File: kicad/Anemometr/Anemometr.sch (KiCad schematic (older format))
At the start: 74 parts, among them J1 Conn_01x01_Female, J10 Z3, J11 Z3, J12 Z4, J13 Z4, J14 SWD, J15 SWC, J16 +12v, J17 GND, J2 Conn_01x01_Female, J3 RST, J4 TxD, J5 RxD, J6 Z1, J7 Z1, J8 Z2, J9 Z2, U1 TS5A3166DBVR, U2 LMV7239, U3 TS5A3166DBVR, U4 TS5A3166DBVR, U5 STM32F103C8Tx, U6 TS5A3166DBVR, U7 LM2734Y, U8 MCP1700-5002E_SOT23, U9 MCP1700-3002E_SOT23, Y1 8MHz

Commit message: изменено:      kicad/Anemometr/Anemometr-cache.lib 	изменено:      kicad/Anemometr/Anemometr.sch 	изменено:      kicad/Anemometr/Anemometr.sch-bak
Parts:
- added C? (x2): 10p, Capacitor_SMD:C_0603_1608Metric, symbol Device:C
- added D?: W5500, Package_QFP:LQFP-48_7x7mm_P0.5mm, symbol My_Library:W5500
- added Y?: 8MHz, Crystal:Crystal_SMD_Qantek_QC5CB-2Pin_5x3.2mm, symbol Device:Crystal
- D1: symbol My_Library:MAX4477 -> Anemometr-rescue:MAX4477-My_Library
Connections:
- net labels added: +3.3VA
- wire segments 145 -> 151
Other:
- moved on the sheet: C1, C10, C11, C12, C13, C14, C15, C16, C17, C18, C19, C2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

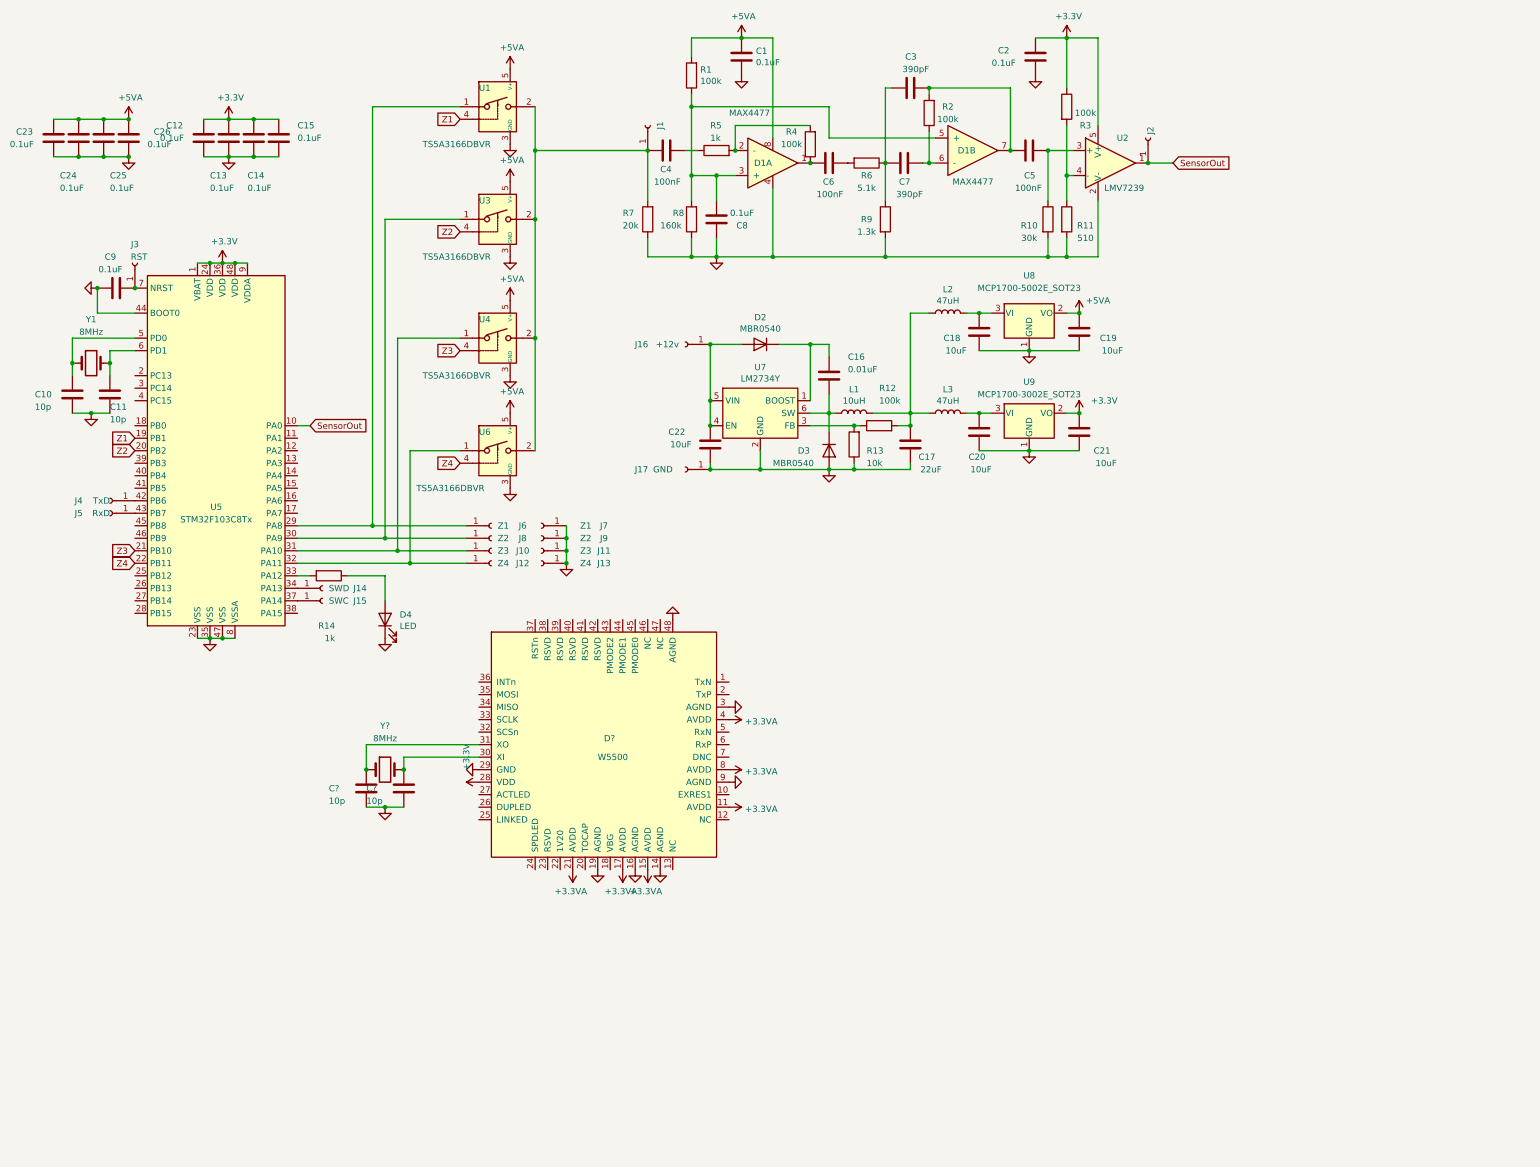
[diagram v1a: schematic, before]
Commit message: изменено:      kicad/Anemometr/Anemometr-cache.lib 	изменено:      kicad/Anemometr/Anemometr.kicad_pcb 	изменено:      kicad/Anemometr/Anemometr.kicad_pcb-bak 	изменено:      kicad/Anemometr/Anemometr.sch 	изменено:      kicad/Anemometr/Anemometr.sch-bak 	изменено:      kicad/Anemometr/fp-info-cache
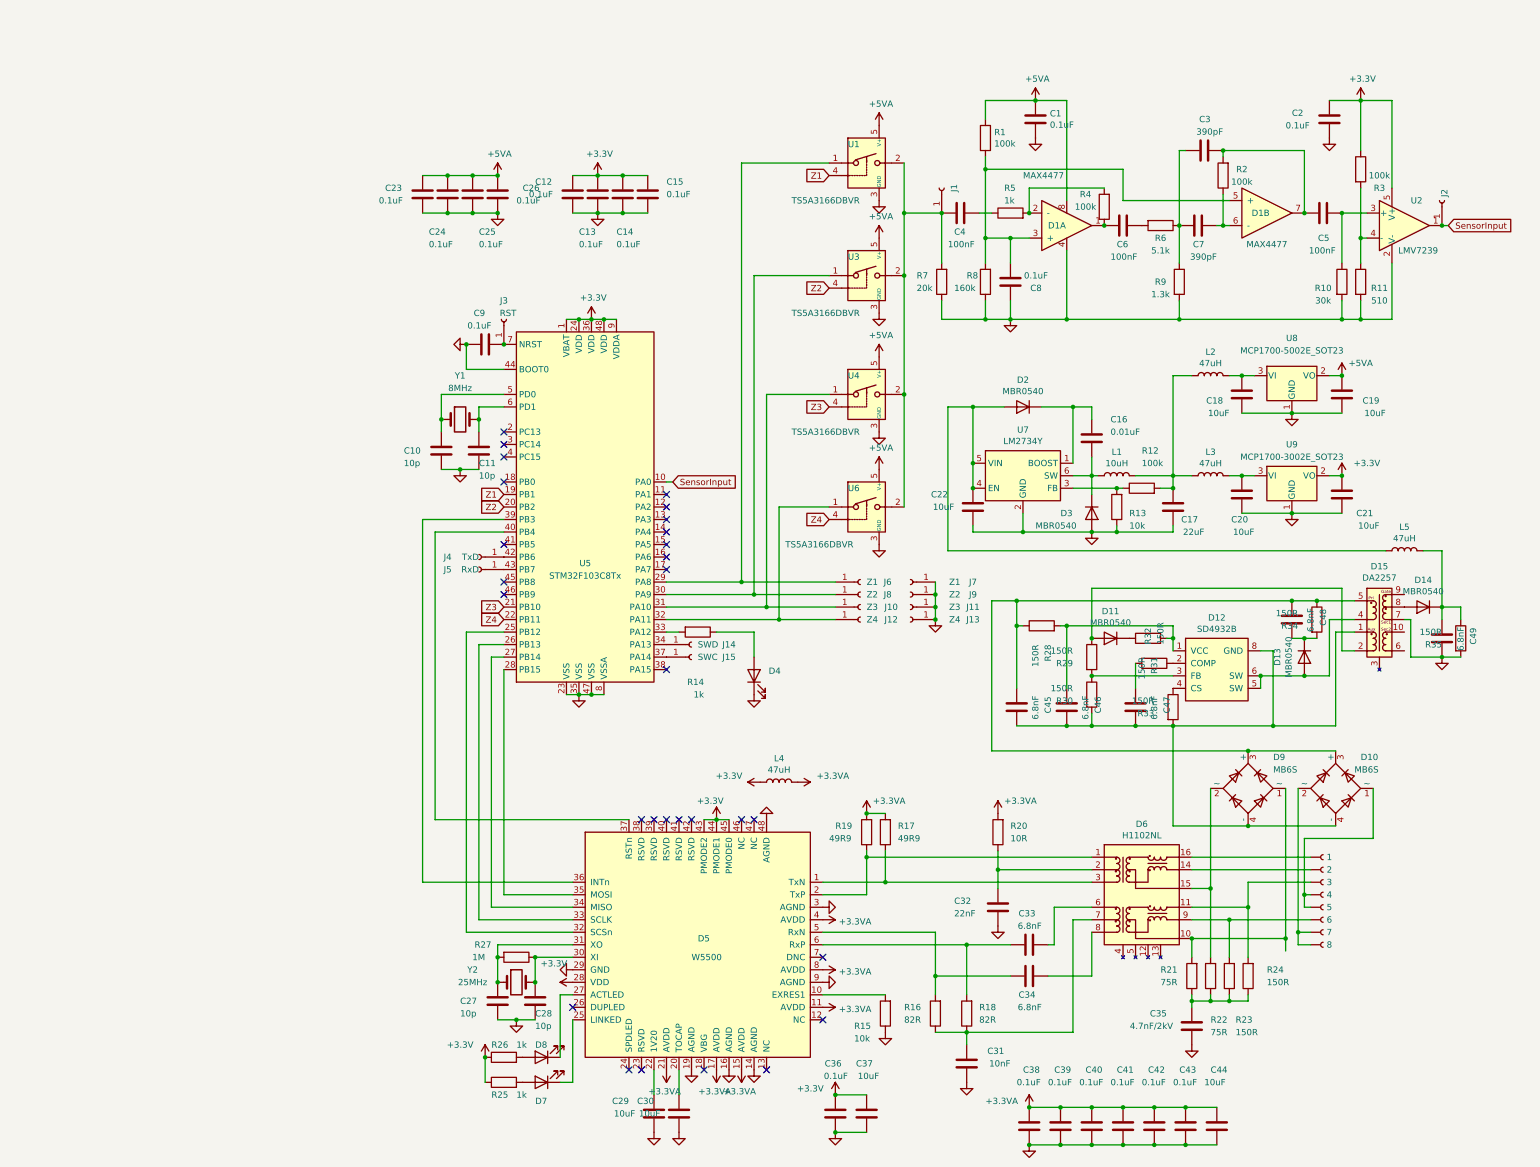
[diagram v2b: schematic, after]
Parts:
- removed J16: +12v, Connector_Pin:Pin_D1.0mm_L10.0mm, symbol Connector:Conn_01x01_Female
- removed J17: GND, Connector_Pin:Pin_D1.0mm_L10.0mm, symbol Connector:Conn_01x01_Female
- added C29, C30, C37, C44: 10uF, Capacitor_SMD:C_0805_2012Metric, symbol Device:C
- added C31: 10nF, Capacitor_SMD:C_0805_2012Metric, symbol Device:C
- added C32: 22nF, Capacitor_SMD:C_0805_2012Metric, symbol Device:C
- added C33, C34, C45, C46, C47, C48, C49: 6.8nF, Capacitor_SMD:C_0805_2012Metric, symbol Device:C
- added C35: 4.7nF/2kV, Capacitor_SMD:C_0805_2012Metric, symbol Device:C
- added C36, C38, C39, C40, C41, C42, C43: 0.1uF, Capacitor_SMD:C_0805_2012Metric, symbol Device:C
- added D10, D9: MB6S, Package_TO_SOT_SMD:TO-269AA, symbol Diode_Bridge:MB6S
- added D11, D13, D14: MBR0540, Diode_SMD:D_SOD-123, symbol Device:D
- added D12: SD4932B, Package_SO:SOIC-8-N7_3.9x4.9mm_P1.27mm, symbol My_Library:SD4932B
- added D15: DA2257, My-library:DA2257, symbol My_Library:DA2257
- added D6: H1102NL, My-library:H1102N, symbol My_Library:H1102NL
- added D7, D8: LED, LED_SMD:LED_0805_2012Metric, symbol Device:LED
- added J18: 1, My-library:SMD-CONN, symbol My_Library:Conn
- added J19: 2, My-library:SMD-CONN, symbol My_Library:Conn
- added J20: 3, My-library:SMD-CONN, symbol My_Library:Conn
- added J21: 4, My-library:SMD-CONN, symbol My_Library:Conn
- added J22: 5, My-library:SMD-CONN, symbol My_Library:Conn
- added J23: 6, My-library:SMD-CONN, symbol My_Library:Conn
- added J24: 7, My-library:SMD-CONN, symbol My_Library:Conn
- added J25: 8, My-library:SMD-CONN, symbol My_Library:Conn
- added L4, L5: 47uH, Inductor_SMD:L_0805_2012Metric, symbol Device:L
- added R15: 10k, Resistor_SMD:R_0805_2012Metric, symbol Device:R
- added R16, R18: 82R, Resistor_SMD:R_0805_2012Metric, symbol Device:R
- added R17, R19: 49R9, Resistor_SMD:R_0805_2012Metric, symbol Device:R
- added R20: 10R, Resistor_SMD:R_0805_2012Metric, symbol Device:R
- added R21, R22: 75R, Resistor_SMD:R_0805_2012Metric, symbol Device:R
- added R23, R24, R28, R29, R30, R31, R32, R33, R34, R35: 150R, Resistor_SMD:R_0805_2012Metric, symbol Device:R
- added R25, R26: 1k, Resistor_SMD:R_0805_2012Metric, symbol Device:R
- added R27: 1M, Resistor_SMD:R_0805_2012Metric, symbol Device:R
- Y2: renamed from Y?; value 8MHz -> 25MHz
- gave numbers to parts that had none: 3
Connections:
- net +3.3VA: now also C38.1, C39.1, C40.1, C41.1, C42.1, C43.1, C44.1, L4.2, R17.2, R19.2, R20.2
- net +3V3: now also D5.43 (PMODE2), D5.44 (PMODE1), D5.45 (PMODE0), C36.2, C37.2, L4.1, R25.1, R26.1
- net GND: now also C29.1, C30.1, C31.1, C32.2, C35.1, C36.1, C37.1, C38.2, C39.2, C40.2, C41.2, C42.2, C43.2, C44.2, C49.2, D15.7, R15.1, R35.2
- net at C22.2, D2.2 (A), U7.4 (EN)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: now also L5.1
- net at U5.25 (PB12): now also D5.32 (SCSn)
- net at U5.26 (PB13): now also D5.33 (SCLK)
- net at U5.27 (PB14): now also D5.34 (MISO)
- net at U5.28 (PB15): now also D5.35 (MOSI)
- net at U5.39 (PB3): now also D5.36 (INTn)
- net at U5.40 (PB4): now also D5.37 (RSTn)
- net at D5.1 (TxN): now also D6.3, R17.1
- net at D5.10 (EXRES1): now also R15.2
- net at D5.2 (TxP): now also D6.1, R19.1
- net at D5.20 (TOCAP): now also C30.2
- net at D5.22 (1V20): now also C29.2
- net at D5.25 (LINKED): now also D7.1 (K)
- net at D5.27 (ACTLED): now also D8.1 (K)
- net at C28.1, D5.30 (XI), Y2.2: now also R27.1
- net at C27.1, D5.31 (XO), Y2.1: now also R27.2
- net at D5.5 (RxN): now also C34.1, R16.2
- net at D5.6 (RxP): now also C33.1, R18.2
- net SensorOut renamed SensorInput
- new net: C32.1, D6.2, R20.1
- new net: C33.2, D6.6
- new net: C34.2, D6.8
- new net: C31.2, D6.7, R16.1, R18.1
- new net: D6.10, D9.1 (~~), R21.2
- new net: D6.11, J20.1, R24.2
- new net: D6.14, J19.1
- new net: D6.15, D9.2 (~~), R22.2
- new net: D6.16, J18.1
- new net: D6.9, J23.1, R23.2
- new net: C35.2, R21.1, R22.1, R23.1, R24.1
- new net: D10.1 (~~), J21.1, J22.1
- new net: D10.2 (~~), J24.1, J25.1
- new net: D8.2 (A), R26.2
- new net: D7.2 (A), R25.2
- new net: C45.1, C48.1, D10.3 (+), D15.5, D9.3 (+), R28.1, R34.1
- new net: C45.2, C46.2, C47.2, D10.4 (-), D12.8 (GND), D15.1, D9.4 (-), R30.2, R33.2
- new net: C46.1, D12.1 (VCC), R28.2, R31.2
- new net: D12.2 (COMP), R32.1
- new net: D12.3 (FB), R29.2, R30.1
- new net: D12.4 (CS), R33.1
- new net: D12.5 (SW), D12.6 (SW), D13.2 (A), D15.4
- new net: D11.1 (K), R31.1
- new net: D11.2 (A), D15.2, R29.1
- new net: C47.1, R32.2
- new net: C48.2, D13.1 (K), R34.2
- new net: C49.1, D14.1 (K), L5.2, R35.1
- new net: D14.2 (A), D15.8
- no-connect marks 0 -> 29
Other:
- moved on the sheet: C1, C10, C11, C12, C13, C14, C15, C16, C17, C18, C19, C2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

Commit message: изменено:      kicad/Anemometr/Anemometr-cache.lib 	изменено:      kicad/Anemometr/Anemometr-rescue.lib 	изменено:      kicad/Anemometr/Anemometr.kicad_pcb 	изменено:      kicad/Anemometr/Anemometr.kicad_pcb-bak 	изменено:      kicad/Anemometr/Anemometr.sch 	изменено:      kicad/Anemometr/Anemometr.sch-bak 	изменено:      kicad/Anemometr/fp-info-cache
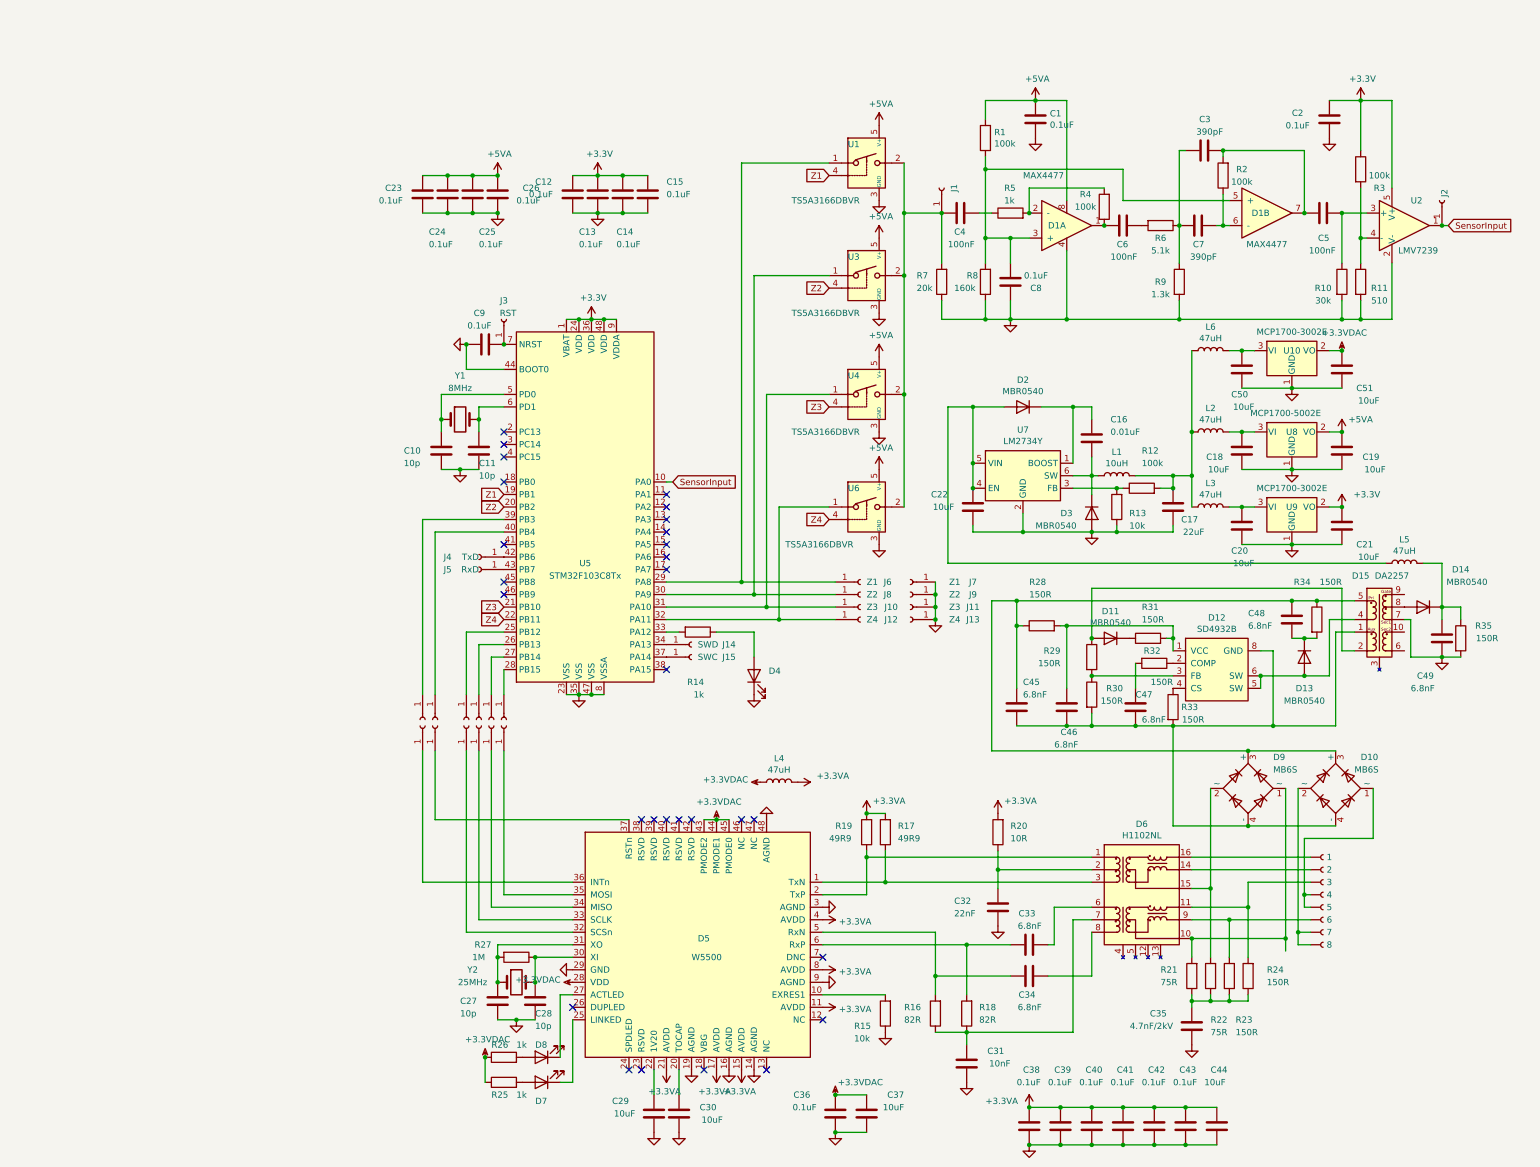
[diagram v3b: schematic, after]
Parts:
- added C50, C51: 10uF, Capacitor_SMD:C_0805_2012Metric, symbol Device:C
- added J16, J17, J26, J27, J28, J29, J30, J31, J32, J33, J34, J35: Z4, My-library:SMD-CONN, symbol Connector:Conn_01x01_Female
- added L6: 47uH, Inductor_SMD:L_0805_2012Metric, symbol Device:L
- added U10: MCP1700-3002E, Package_TO_SOT_SMD:SOT-23, symbol Regulator_Linear:MCP1700-3002E_SOT23
- C29, C30, C31, C32, C33, C34, C36, C37, C38, C39, C40, C41, C42, C43, C44, C47, C48: footprint Capacitor_SMD:C_0805_2012Metric -> Capacitor_SMD:C_0603_1608Metric
- D7, D8: footprint LED_SMD:LED_0805_2012Metric -> LED_SMD:LED_0603_1608Metric
- J10, J11, J12, J13, J6, J7, J8, J9: footprint Connector_Pin:Pin_D1.0mm_L10.0mm -> My-library:SMD-CONN
- R15, R16, R18, R20, R21, R22, R23, R24, R25, R26, R27: footprint Resistor_SMD:R_0805_2012Metric -> Resistor_SMD:R_0402_1005Metric
- R17, R19, R28, R29, R30, R31, R32, R33, R34, R35: footprint Resistor_SMD:R_0805_2012Metric -> Resistor_SMD:R_0603_1608Metric
- U8: value MCP1700-5002E_SOT23 -> MCP1700-5002E
- U9: value MCP1700-3002E_SOT23 -> MCP1700-3002E
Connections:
- net +3V3: no longer C36.2, C37.2, D5.28 (VDD), D5.43 (PMODE2), D5.44 (PMODE1), D5.45 (PMODE0), L4.1, R25.1, R26.1
- net GND: now also C50.1, C51.1, U10.1 (GND)
- net at C17.2, L1.2, L2.1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: now also L6.1
- net at U5.25 (PB12): now also J28.1 (Pin_1); no longer D5.32 (SCSn)
- net at U5.26 (PB13): now also J30.1 (Pin_1); no longer D5.33 (SCLK)
- net at U5.27 (PB14): now also J32.1 (Pin_1); no longer D5.34 (MISO)
- net at U5.28 (PB15): now also J34.1 (Pin_1); no longer D5.35 (MOSI)
- net at U5.39 (PB3): now also J16.1 (Pin_1); no longer D5.36 (INTn)
- net at U5.40 (PB4): now also J26.1 (Pin_1); no longer D5.37 (RSTn)
- new net: D5.32 (SCSn), J29.1 (Pin_1)
- new net: D5.33 (SCLK), J31.1 (Pin_1)
- new net: D5.34 (MISO), J33.1 (Pin_1)
- new net: D5.35 (MOSI), J35.1 (Pin_1)
- new net: D5.36 (INTn), J17.1 (Pin_1)
- new net: D5.37 (RSTn), J27.1 (Pin_1)
- new net: C50.2, L6.2, U10.3 (VI)
- new net +3.3VDAC: C36.2, C37.2, C51.2, D5.28 (VDD), D5.43 (PMODE2), D5.44 (PMODE1), D5.45 (PMODE0), L4.1, R25.1, R26.1, U10.2 (VO)
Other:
- moved on the sheet: C18, C19, C20, C21, L2, L3, L5, U8, U9

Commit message: изменено:      kicad/Anemometr/Anemometr-cache.lib 	изменено:      kicad/Anemometr/Anemometr.sch 	изменено:      kicad/Anemometr/Anemometr.sch-bak
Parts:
- D12: symbol My_Library:SD4932B -> Anemometr-rescue:SD4932B-My_Library
- D15: symbol My_Library:DA2257 -> Anemometr-rescue:DA2257-My_Library
- D5: symbol My_Library:W5500 -> Anemometr-rescue:W5500-My_Library
- D6: symbol My_Library:H1102NL -> Anemometr-rescue:H1102NL-My_Library
- J18, J19, J20, J21, J22, J23, J24, J25: symbol My_Library:Conn -> Anemometr-rescue:Conn-My_Library
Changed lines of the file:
@@
 Z1
 $Comp
-L My_Library:W5500 D5
+L Anemometr-rescue:W5500-My_Library D5
 U 1 1 61EEF122
 P 6150 8000
@@
 Connection ~ 8150 8650
 $Comp
-L My_Library:H1102NL D6
+L Anemometr-rescue:H1102NL-My_Library D6
 U 1 1 61F6B654
 P 9550 7550
@@
 $EndComp
 $Comp
-L My_Library:Conn J18
+L Anemometr-rescue:Conn-My_Library J18
 U 1 1 6201FB36
 P 11000 7250
@@
 $EndComp
 $Comp
-L My_Library:Conn J19
+L Anemometr-rescue:Conn-My_Library J19
 U 1 1 620202BB
 P 11000 7350
@@
 $EndComp
 $Comp
-L My_Library:Conn J20
+L Anemometr-rescue:Conn-My_Library J20
 U 1 1 620208F4
 P 11000 7450
@@
 $EndComp
 $Comp
-L My_Library:Conn J21
+L Anemometr-rescue:Conn-My_Library J21
 U 1 1 62020F8F
 P 11000 7550
@@
 $EndComp
 $Comp
-L My_Library:Conn J22
+L Anemometr-rescue:Conn-My_Library J22
 U 1 1 620215DE
 P 11000 7650
@@
 $EndComp
 $Comp
-L My_Library:Conn J23
+L Anemometr-rescue:Conn-My_Library J23
 U 1 1 62021C50
 P 11000 7750
@@
 $EndComp
 $Comp
-L My_Library:Conn J24
+L Anemometr-rescue:Conn-My_Library J24
 U 1 1 62022327
 P 11000 7850
@@
 $EndComp
 $Comp
-L My_Library:Conn J25
+L Anemometr-rescue:Conn-My_Library J25
 U 1 1 62022978
 P 11000 7950
@@
 	10400 6400 11100 6400
 $Comp
-L My_Library:SD4932B D12
+L Anemometr-rescue:SD4932B-My_Library D12
 U 1 1 629D5E4E
 P 10150 5750
@@
 $EndComp
 $Comp
-L My_Library:DA2257 D15
+L Anemometr-rescue:DA2257-My_Library D15
 U 1 1 622C6996
 P 11450 5400
